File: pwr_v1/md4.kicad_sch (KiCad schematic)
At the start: 17 parts, among them M4 Conn_01x08_Socket

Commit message: Schematic and layout updated
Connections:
- net GNDREF: no longer 4C6.2, 4U1.4 (GND_BK), M4.4 (Pin_4)
- new net GND_BK: 4C6.2, 4U1.4 (GND_BK), M4.4 (Pin_4)
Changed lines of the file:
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@@
 	)
 	(junction
-		(at 138.684 46.609)
-		(diameter 0)
-		(color 0 0 0 0)
-	)
-	(junction
-		(at 125.984 46.609)
-		(diameter 0)
-		(color 0 0 0 0)
-	)
-	(junction
 		(at 204.724 81.28)
 		(diameter 0)
@@
 	)
 	(junction
-		(at 204.724 66.04)
-		(diameter 0)
-		(color 0 0 0 0)
-	)
-	(junction
 		(at 204.724 73.66)
 		(diameter 0)
@@
 	(wire
 		(pts
-			(xy 197.104 88.9) (xy 197.104 90.17)
-		)
-		(stroke
-			(width 0)
-			(type default)
-		)
-	)
-	(wire
-		(pts
 			(xy 132.334 46.609) (xy 132.334 53.34)
 		)
@@
 	(wire
 		(pts
-			(xy 204.724 46.609) (xy 138.684 46.609)
-		)
-		(stroke
-			(width 0)
-			(type default)
-		)
-	)
-	(wire
-		(pts
 			(xy 145.034 107.95) (xy 145.034 116.84)
 		)
@@
 	(wire
 		(pts
-			(xy 120.65 46.609) (xy 125.984 46.609)
-		)
-		(stroke
-			(width 0)
-			(type default)
-		)
-	)
-	(wire
-		(pts
 			(xy 147.574 114.3) (xy 151.384 114.3)
 		)
@@
 	(wire
 		(pts
-			(xy 204.724 46.609) (xy 204.724 66.04)
-		)
-		(stroke
-			(width 0)
-			(type default)
-		)
-	)
-	(wire
-		(pts
 			(xy 139.954 107.95) (xy 145.034 107.95)
 		)
@@
 	(text "AVDD 3.3V/30mA"
 		(exclude_from_sim no)
-		(at 182.753 46.355 0)
+		(at 205.486 66.548 0)
 		(effects
 			(font
@@
 	)
 	(label "AVDD"
-		(at 120.65 46.609 0)
+		(at 125.984 46.736 0)
 		(fields_autoplaced yes)
 		(effects
@@
 					(unit 1)
 				)
-			)
-		)
-	)
-	(symbol
-		(lib_id "power:GNDREF")
-		(at 197.104 90.17 0)
-		(unit 1)
-		(exclude_from_sim no)
-		(in_bom yes)
-		(on_board yes)
-		(dnp no)
-		(property "Reference" "#PWR041"
-			(at 197.104 96.52 0)
-			(effects
-				(font
-					(size 1.27 1.27)
-				)
-				(hide yes)
-			)
-		)
-		(property "Value" "GNDREF"
-			(at 197.104 93.98 0)
-			(effects
-				(font
-					(size 1.27 1.27)
-				)
-				(hide yes)
-			)
-		)
-		(property "Footprint" ""
-			(at 197.104 90.17 0)
-			(effects
-				(font
-					(size 1.27 1.27)
-				)
-				(hide yes)
-			)
-		)
-		(property "Datasheet" ""
-			(at 197.104 90.17 0)
-			(effects
-				(font
-					(size 1.27 1.27)
-				)
-				(hide yes)
-			)
-		)
-		(property "Description" ""
-			(at 197.104 90.17 0)
-			(effects
-				(font
-					(size 1.27 1.27)
-				)
-				(hide yes)
-			)
-		)
-		(pin "1"
-		)
-		(instances
-			(project "pwr_v1"
-				(path "/42eee4f9-ea65-4e89-8296-df9554a24009/685a8965-c929-484c-bc22-0221d7d480eb"
-					(reference "#PWR041")
-					(unit 1)
-				)

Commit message: Schematic updated
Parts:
- 4C1: footprint Capacitor_SMD:C_0805_2012Metric -> Capacitor_SMD:C_0402_1005Metric
- 4C2, 4C4, 4C6: footprint Capacitor_SMD:C_0603_1608Metric -> Capacitor_SMD:C_0402_1005Metric
- 4R1: footprint Resistor_SMD:R_0603_1608Metric_Pad0.98x0.95mm_HandSolder -> Resistor_SMD:R_0603_1608Metric

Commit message: Sch and Layout updated; Added batt sup ckt, placed and routed all motor drivers.
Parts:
- M4: footprint Connector_PinHeader_2.54mm:PinHeader_1x08_P2.54mm_Vertical_SMD_Pin1Left -> Connector_PinHeader_2.54mm:PinHeader_1x08_P2.54mm_Vertical
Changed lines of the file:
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@@
 			)
 		)
-		(property "Footprint" "Connector_PinHeader_2.54mm:PinHeader_1x08_P2.54mm_Vertical_SMD_Pin1Left"
+		(property "Footprint" "Connector_PinHeader_2.54mm:PinHeader_1x08_P2.54mm_Vertical"
 			(at 255.524 107.95 0)
 			(effects

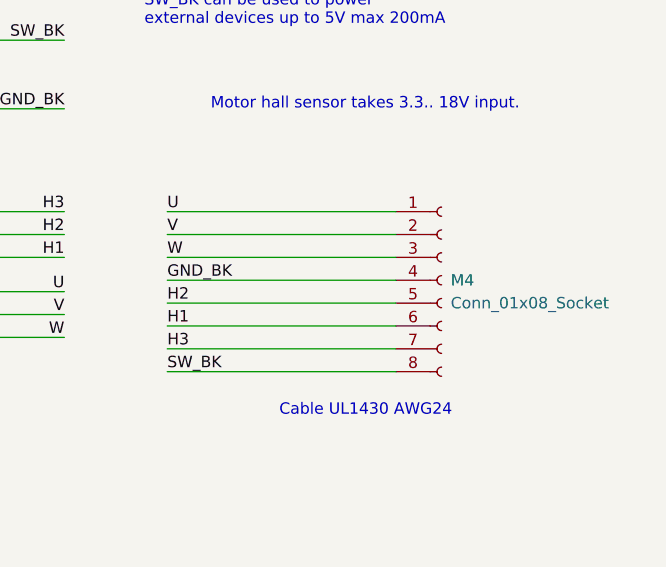
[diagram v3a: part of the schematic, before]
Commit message: Schematic and layout updated; Motor driver alignments and planes;  Few components updated
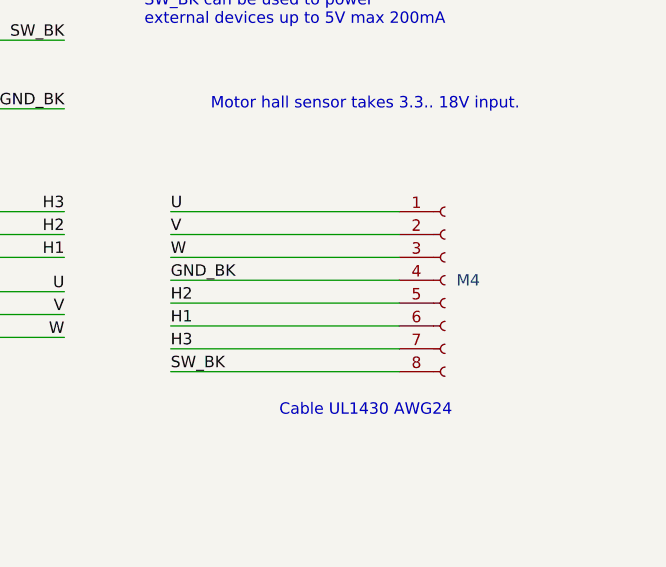
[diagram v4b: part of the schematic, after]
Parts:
- M4: footprint Connector_PinHeader_2.54mm:PinHeader_1x08_P2.54mm_Vertical -> Connector_Molex:Molex_KK-254_AE-6410-08A_1x08_P2.54mm_Vertical
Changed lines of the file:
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@@
 	(wire
 		(pts
-			(xy 225.044 100.33) (xy 250.444 100.33)
+			(xy 225.425 100.33) (xy 250.825 100.33)
 		)
 		(stroke
@@
 	(wire
 		(pts
-			(xy 225.044 118.11) (xy 250.444 118.11)
+			(xy 225.425 118.11) (xy 250.825 118.11)
 		)
 		(stroke
@@
 	(wire
 		(pts
-			(xy 225.044 102.87) (xy 250.444 102.87)
-		)
-		(stroke
-			(width 0)
-			(type default)
-		)
-	)
-	(wire
-		(pts
-			(xy 225.044 105.41) (xy 250.444 105.41)
+			(xy 225.425 102.87) (xy 250.825 102.87)
+		)
+		(stroke
+			(width 0)
+			(type default)
+		)
+	)
+	(wire
+		(pts
+			(xy 225.425 105.41) (xy 250.825 105.41)
 		)
 		(stroke
@@
 	(wire
 		(pts
-			(xy 225.044 107.95) (xy 250.444 107.95)
+			(xy 225.425 107.95) (xy 250.825 107.95)
 		)
 		(stroke
@@
 	(wire
 		(pts
-			(xy 225.044 115.57) (xy 250.444 115.57)
+			(xy 225.425 115.57) (xy 250.825 115.57)
 		)
 		(stroke
@@
 	(wire
 		(pts
-			(xy 225.044 110.49) (xy 250.444 110.49)
+			(xy 225.425 110.49) (xy 250.825 110.49)
 		)
 		(stroke
@@
 	(wire
 		(pts
-			(xy 225.044 113.03) (xy 250.444 113.03)
+			(xy 225.425 113.03) (xy 250.825 113.03)
 		)
 		(stroke
@@
 	)
 	(label "H2"
-		(at 225.044 110.49 0)
+		(at 225.425 110.49 0)
 		(fields_autoplaced yes)
 		(effects
@@
 	)
 	(label "SW_BK"
-		(at 225.044 118.11 0)
+		(at 225.425 118.11 0)
 		(fields_autoplaced yes)
 		(effects
@@
 	)
 	(label "H3"
-		(at 225.044 115.57 0)
+		(at 225.425 115.57 0)
 		(fields_autoplaced yes)
 		(effects
@@
 	)
 	(label "V"
-		(at 225.044 102.87 0)
+		(at 225.425 102.87 0)
 		(fields_autoplaced yes)
 		(effects
@@
 	)
 	(label "H1"
-		(at 225.044 113.03 0)
+		(at 225.425 113.03 0)
 		(fields_autoplaced yes)
 		(effects
@@
 	)
 	(label "GND_BK"
-		(at 225.044 107.95 0)
+		(at 225.425 107.95 0)
 		(fields_autoplaced yes)
 		(effects
@@
 	)
 	(label "W"
-		(at 225.044 105.41 0)
+		(at 225.425 105.41 0)
 		(fields_autoplaced yes)
 		(effects
@@
 	)
 	(label "U"
-		(at 225.044 100.33 0)
+		(at 225.425 100.33 0)
 		(fields_autoplaced yes)
 		(effects
@@
 	)
 	(symbol
+		(lib_id "Connector:Conn_01x08_Socket")
+		(at 255.905 107.95 0)
+		(unit 1)
+		(exclude_from_sim no)
+		(in_bom yes)
+		(on_board yes)
+		(dnp no)
+		(fields_autoplaced yes)
+		(property "Reference" "M4"
+			(at 257.175 107.9499 0)
+			(effects
+				(font
+					(size 1.27 1.27)
+				)
+				(justify left)
+			)
+		)
+		(property "Value" "Conn_01x08_Socket"
+			(at 257.175 110.4899 0)
+			(effects
+				(font
+					(size 1.27 1.27)
+				)
+				(justify left)
+				(hide yes)
+			)
+		)
+		(property "Footprint" "Connector_Molex:Molex_KK-254_AE-6410-08A_1x08_P2.54mm_Vertical"
+			(at 255.905 107.95 0)
+			(effects
+				(font
+					(size 1.27 1.27)
+				)
+				(hide yes)
+			)
+		)
+		(property "Datasheet" "~"
+			(at 255.905 107.95 0)
+			(effects
+				(font
+					(size 1.27 1.27)
+				)
+				(hide yes)
+			)
+		)
+		(property "Description" ""
+			(at 255.905 107.95 0)
+			(effects
+				(font
+					(size 1.27 1.27)
+				)
+				(hide yes)
+			)
+		)
+		(pin "2"
+		)
+		(pin "7"
+		)
+		(pin "3"
+		)
+		(pin "1"
+		)
+		(pin "8"
+		)
+		(pin "5"
+		)
+		(pin "4"
+		)
+		(pin "6"
+		)
+		(instances
+			(project "pwr_v1"
+				(path "/42eee4f9-ea65-4e89-8296-df9554a24009/685a8965-c929-484c-bc22-0221d7d480eb"
+					(reference "M4")
+					(unit 1)
+				)
+			)
+		)
+	)
+	(symbol
 		(lib_id "Device:C_Small")
 		(at 197.104 85.09 0)
@@
 					(unit 1)
 				)
-			)
-		)
-	)
-	(symbol
-		(lib_id "Connector:Conn_01x08_Socket")
-		(at 255.524 107.95 0)
-		(unit 1)
-		(exclude_from_sim no)
-		(in_bom yes)
-		(on_board yes)
-		(dnp no)
-		(fields_autoplaced yes)
-		(property "Reference" "M4"
-			(at 256.54 107.9499 0)
-			(effects
-				(font
-					(size 1.27 1.27)
-				)
-				(justify left)
-			)
-		)
-		(property "Value" "Conn_01x08_Socket"
-			(at 256.54 110.4899 0)
-			(effects
-				(font
-					(size 1.27 1.27)
-				)
-				(justify left)
-			)
-		)
-		(property "Footprint" "Connector_PinHeader_2.54mm:PinHeader_1x08_P2.54mm_Vertical"
-			(at 255.524 107.95 0)
-			(effects
-				(font
-					(size 1.27 1.27)
-				)
-				(hide yes)
-			)
-		)
-		(property "Datasheet" "~"
-			(at 255.524 107.95 0)
-			(effects
-				(font
-					(size 1.27 1.27)
-				)
-				(hide yes)
-			)
-		)
-		(property "Description" "MFR.Part # X6511WVS-08H-C60D48R2 JLCPCB Part # C2883765"
-			(at 255.524 107.95 0)
-			(effects
-				(font
-					(size 1.27 1.27)
-				)
-				(hide yes)
-			)
-		)
-		(pin "2"
-		)
-		(pin "7"
-		)
-		(pin "3"
-		)
-		(pin "1"
-		)
-		(pin "8"
-		)
-		(pin "5"
-		)
-		(pin "4"
-		)
-		(pin "6"
-		)
-		(instances
-			(project "pwr_v1"
-				(path "/42eee4f9-ea65-4e89-8296-df9554a24009/685a8965-c929-484c-bc22-0221d7d480eb"
-					(reference "M4")
-					(unit 1)
-				)

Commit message: Schematic and layout updated; Layout placement and routing completed
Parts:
- M4: footprint Connector_Molex:Molex_KK-254_AE-6410-08A_1x08_P2.54mm_Vertical -> Connector_PinHeader_2.54mm:PinHeader_1x08_P2.54mm_Vertical

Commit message: Sch: 0ohm res added to SPI pins, MD footprints updated; Lay: Silkscreen aligned, logo added, DRC
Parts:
- 4U1: footprint MTR:RGF0040E-IPC_B -> motorDriver:RGF0040E-IPC_B
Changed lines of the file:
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@@
 			)
 		)
-		(property "Footprint" "MTR:RGF0040E-IPC_B"
+		(property "Footprint" "motorDriver:RGF0040E-IPC_B"
 			(at 227.584 58.42 0)
 			(effects

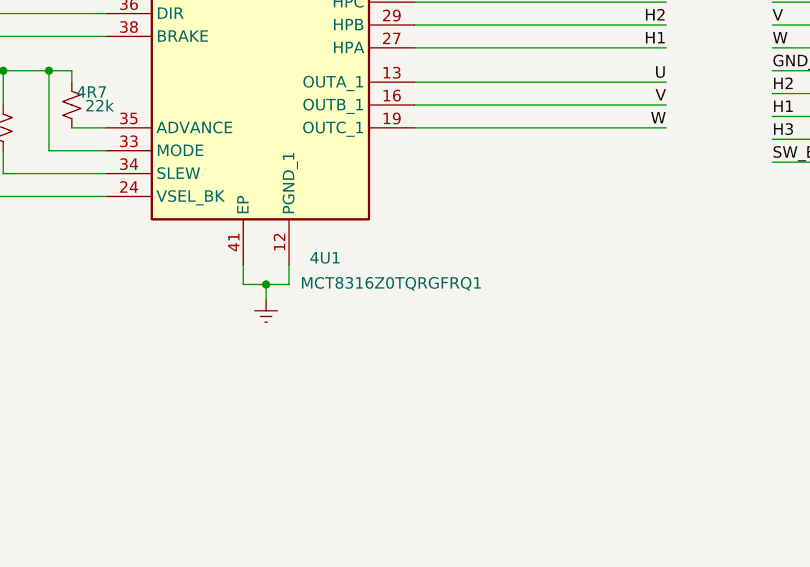
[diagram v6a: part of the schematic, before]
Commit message: Sch: DNP updated, JLC part numbers updated for all components; Lay: Fiducial placement, routing aligned.
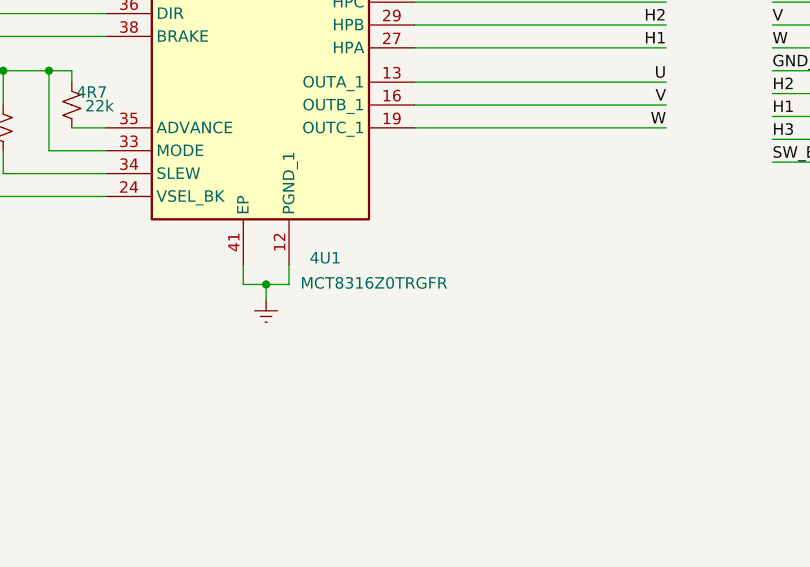
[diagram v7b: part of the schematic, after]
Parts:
- 4U1: value MCT8316Z0TQRGFRQ1 -> MCT8316Z0TRGFR
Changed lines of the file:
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@@
 			)
 		)
-		(property "Description" "Resistor, small US symbol"
+		(property "Description" "MFR.Part # 0603WAF2002T5E JLCPCB Part # C4184"
 			(at 138.684 69.85 0)
 			(effects
@@
 			)
 		)
-		(property "Description" ""
+		(property "Description" "MFR.Part # HB-PH3-25418PB2GOP JLCPCB Part # C6332201"
 			(at 255.905 107.95 0)
 			(effects
@@
 			)
 		)
-		(property "Description" "Resistor, small US symbol"
+		(property "Description" "MFR.Part # RC0805FR-071ML JLCPCB Part # C107700"
 			(at 133.604 114.3 0)
 			(effects
@@
 			)
 		)
-		(property "Description" "Resistor, small US symbol"
+		(property "Description" "MFR.Part # 0402WGF4702TCE JLCPCB Part # C25792"
 			(at 139.954 114.3 0)
 			(effects
@@
 			)
 		)
-		(property "Description" "Resistor, small US symbol"
+		(property "Description" "MFR.Part # 0402WGJ0223TCE JLCPCB Part # C25547"
 			(at 147.574 111.76 0)
 			(effects
@@
 			)
 		)
-		(property "Description" "Resistor, small US symbol"
+		(property "Description" "MFR.Part # 0603WAF2702T5E JLCPCB Part # C22967"
 			(at 138.684 55.88 0)
 			(effects
@@
 			)
 		)
-		(property "Value" "MCT8316Z0TQRGFRQ1"
+		(property "Value" "MCT8316Z0TRGFR"
 			(at 172.974 131.572 0)
 			(effects
@@
 			)
 		)
-		(property "Description" ""
+		(property "Description" "MFR.Part # MCT8316Z0TRGFR JLCPCB Part # C3681342"
 			(at 151.384 71.12 0)
 			(effects

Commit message: Final PCB files sent for fab
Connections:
- net GNDREF renamed GND
